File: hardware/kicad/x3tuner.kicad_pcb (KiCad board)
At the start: 2 copper layers, 38 x 60 mm, 53 parts, among them J1 USB-C, J2 AKKU, J3 SWD-ZIEL, Q1 AO3401A, Q2 HJ8205, SW1 EIN/AUS, SW2 RESET, SW3 BOOT, U1 ESP32-S3-WROOM-1-N16R8, U2 TP4056, U3 DW01A, U4 ME6211C33M5G-N, U5 ME6211C33M5G-N, U6 SRV05-4

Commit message: Add 10-up production panel and volume cost estimate
JLCPCB's Economic assembly is limited to 2-50 pieces and Standard
assembly needs boards >= 70 x 70 mm, so 100-500 units need a panel:

- gen/make_panel.py builds a 5x2 KiKit panel (202 x 139 mm, mouse-bite
  tabs, rails with fiducials/tooling holes, top row rotated so all SWD
  edges face the rails); DRC clean; Gerber/BOM/CPL in production/panel
- tab positions come from kikit:Tab annotations (circuit.PANEL_TABS),
  placed clear of the USB-C, switch and SWD header edges
- ESP32 module footprint: antenna keep-out/courtyard trimmed to the
  38 mm board so it no longer spills into neighbouring panel boards
- README: cost per board for 100/200/500 pcs, complete-device cost,
  EU compliance notes for selling

Co-Authored-By: Claude Opus 5.5 <noreply@anthropic.com>
Claude-Session: https://claude.ai/code/session_01RVwXhv4cRLa5H5kfiVg79q
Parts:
- added KT1: Tab, kikit:Tab, F.Cu at (101.5, 75.0)
- added KT2: Tab, kikit:Tab, F.Cu at (101.5, 105.0)
- added KT3: Tab, kikit:Tab, F.Cu at (136.5, 75.0)
- added KT4: Tab, kikit:Tab, F.Cu at (136.5, 105.0)
- added KT5: Tab, kikit:Tab, F.Cu at (119.0, 61.5)
- added KT6: Tab, kikit:Tab, F.Cu at (114.5, 118.5)

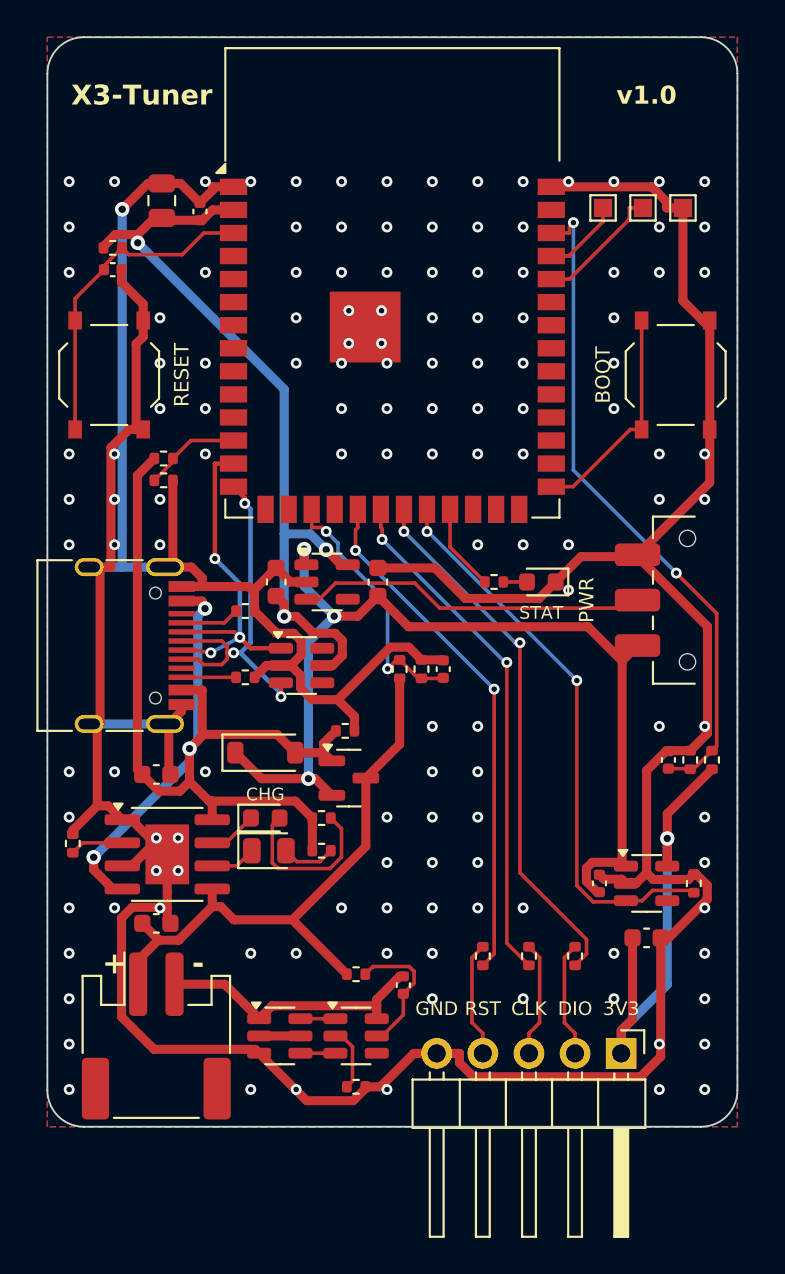
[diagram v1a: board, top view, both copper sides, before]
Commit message: Cost-down rev 1.1: ESP32-C3-WROOM-02 and MSK12C02 switch
Swap the ESP32-S3-WROOM-1-N16R8 for an ESP32-C3-WROOM-02-N4 (about
1.20-1.55 USD less per board at 100+) and the C&K slide switch for an
MSK12C02 (about 0.55 USD less), roughly 30 % off the assembled board.

- new pin plan: SWD on IO5/6/7, sense inputs on ADC1 (IO1/IO3/IO4),
  TGT_EN IO10, LED IO0, BOOT IO9, 10k pull-ups on strapping IO2/IO8
- USB-C moves to the right edge (USB pre-route generalised for either
  orientation), switch to the left; board shrinks to 38 x 54.5 mm
- project footprints: C3 module without 0.2 mm EPAD vias and with a
  board-sized antenna keep-out; MSK12C02 land pattern after the EasyEDA
  footprint for C431540
- re-routed, DRC clean (board and 10-up panel, now 202 x 128 mm)
- case follows the board: side-agnostic ports, 503040 battery bay,
  42 x 65 x 17 mm
- firmware: x3tuner env now targets esp32-c3 with the new pin map
- docs: updated cost tables (about 5.20/4.80/4.50 USD per board at
  100/200/500 incl. VAT), verification notes

Co-Authored-By: Claude Opus 5.5 <noreply@anthropic.com>
Claude-Session: https://claude.ai/code/session_01RVwXhv4cRLa5H5kfiVg79q
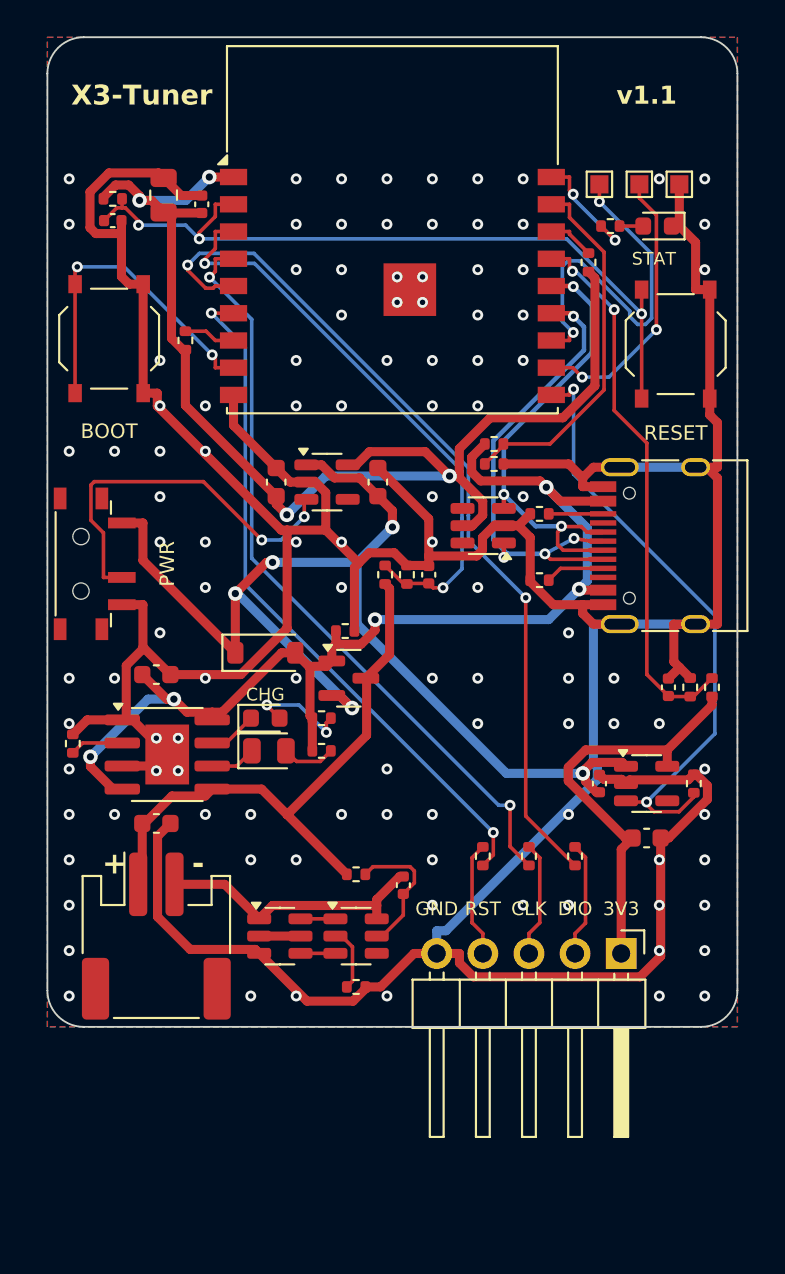
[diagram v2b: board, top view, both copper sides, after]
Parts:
- added R21: 10k, Resistor_SMD:R_0402_1005Metric, F.Cu at (107.6, 76.7)
- added R22: 10k, Resistor_SMD:R_0402_1005Metric, F.Cu at (129.8, 72.4)
- SW1: footprint Button_Switch_SMD:SW_SPDT_CK_JS102011SAQN -> x3tuner:SW_SPDT_MSK12C02
- U1: value ESP32-S3-WROOM-1-N16R8 -> ESP32-C3-WROOM-02-N4; footprint x3tuner:ESP32-S3-WROOM-1_JLC -> x3tuner:ESP32-C3-WROOM-02_JLC
- moved SW1 32.9 mm to (102.4, 89.0), turned to -90 degrees
- moved J1 31.8 mm to (134.7, 88.0), turned to 90 degrees
- moved SW3 31.3 mm to (103.4, 76.6)
- moved SW2 31.2 mm to (134.6, 76.9)
- moved R20 20.6 mm to (131.0, 70.4)
- moved D4 20.6 mm to (133.6, 70.4)
- moved R2 18.5 mm to (127.1, 86.2), turned to 180 degrees
- moved R19 18.2 mm to (124.6, 83.5)
- moved R18 18.2 mm to (124.6, 82.4)
- moved R1 16.3 mm to (127.1, 89.9), turned to 180 degrees
- moved U6 12.6 mm to (124.0, 86.9), turned to 180 degrees
- moved C10 5.50 mm to (133.0, 104.1)
- moved C4 5.50 mm to (106.0, 95.1)
- moved C5 5.50 mm to (106.0, 103.3)
- moved C6 5.50 mm to (119.6, 106.7)
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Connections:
- U1 pad 1: GND -> +3V3
- U1 pad 10: (no net) -> TGT_EN
- U1 pad 11: (no net) -> RXD0
- U1 pad 12: VBUS_SENSE -> TXD0
- U1 pad 15: (no net) -> VTGT_SENSE
- U1 pad 16: (no net) -> STRAP_IO2
- U1 pad 17: VBAT_SENSE -> VBUS_SENSE
- U1 pad 18: (no net) -> LED
- U1 pad 19: NRST -> GND
- U1 pad 2: +3V3 -> EN
- U1 pad 3: EN -> VBAT_SENSE
- U1 pad 4: (no net) -> SWCLK
- U1 pad 5: (no net) -> SWDIO
- U1 pad 6: (no net) -> NRST
- U1 pad 7: (no net) -> STRAP_IO8
- U1 pad 8: (no net) -> BOOT
- U1 pad 9: (no net) -> GND
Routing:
- net +3V3: track 44.0 -> 69.3 mm, vias 3 -> 4
- net EN: track 17.9 -> 42.2 mm, vias 0 -> 3
- net SWDIO: track 29.7 -> 48.2 mm
- net VBAT_SENSE: track 14.6 -> 32.5 mm
- net TXD0: track 4.42 -> 20.8 mm, vias 0 -> 2
- net VBUS_SENSE: track 5.37 -> 20.3 mm
- net SWCLK: track 28.5 -> 42.2 mm
- net NRST: track 28.6 -> 38.3 mm
- net VSYS: track 55.3 -> 64.5 mm, vias 3 -> 5
- net GND: track 250.3 -> 241.7 mm, vias 136 -> 108
- net RXD0: track 7.04 -> 15.5 mm, vias 0 -> 2
- net VTGT_SENSE: track 36.9 -> 30.3 mm
- net USB_DN: track 20.4 -> 26.9 mm, vias 3 -> 4
- net VBUS: track 67.7 -> 61.5 mm, vias 3 -> 5
- net BOOT: track 12.3 -> 18.2 mm, vias 0 -> 2
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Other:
- board size 38 x 60 mm -> 38 x 54.5 mm
- board text added: "ESP32-C3 SWD-Programmer"
- board text added: "X3-Tuner v1.1"
- board text added: "v1.1"
- board text removed: "ESP32-S3 SWD-Programmer"
- board text removed: "X3-Tuner v1.0"
- board text removed: "v1.0"

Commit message: Cut JLC assembly cost, assemble every part, price with live JLC data
Checked every BOM line live on jlcpcb.com (price, stock, library type):
- U6: ProTek SRV05-4 (C85364) was out of stock (pre-order, MOQ 30);
  now the pin-identical TECH PUBLIC SRV05-4 (C558418, 219k in stock).
- D4: the yellow LED is an extended part (+$3 fee); now the basic white
  KT-0603W (C2290) with a 100 R series resistor.
- J3: the SWD header is now assembled by JLC as well (C32713264, THT),
  so the board needs no hand soldering at all.

The README cost section now uses the live part prices, the PCB price and
shipping from the JLC quote page, and the official fee schedule (10
extended part types, hand-soldering fee for J3). CPL rotations are
normalised to 0..360.

Co-Authored-By: Claude Opus 5.5 <noreply@anthropic.com>
Claude-Session: https://claude.ai/code/session_01RVwXhv4cRLa5H5kfiVg79q
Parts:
- D4: value yellow -> white
- R20: value 1k -> 100
